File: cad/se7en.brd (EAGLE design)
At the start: 64 x 34 mm, 67 parts, among them CN1 MICROSD-EJECT, CN3 DO NOT PLACE, CN4 DO NOT PLACE, CN5 DO NOT PLACE, CN8 HEADER-1X2-THM, Q1 FDC6392S, SW1 SWITCHKMR211, SW2 SWITCHKMR211, U1 ATSAMS70, U2 MCP73831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

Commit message: tweak
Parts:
- CN2: device adafruit:JST-PH-2-SMT-RA -> jaw:JST-PH-2-SMT-RA
- USB1: value CON-USB-F-MICRO-B -> USB-F-B-MICRO-B-192; device dp_devices:CONN_USB_MICRO-B -> jaw:USB-MICRO-B-192
- turned CN2 to 270 degrees

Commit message: usb improve Zd
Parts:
- CN8: value HEADER-1X2-THM -> HEADER-1X2M254; device jaw:HEADER-1X2-THM -> jaw:HEADER-1X2-THM-TIGHT
- moved C1 0.50 mm to (89.0, 64.5)
- moved C13 0.50 mm to (95.0, 64.5)
- moved C16 0.50 mm to (87.0, 64.5)
- moved C17 0.50 mm to (92.5, 64.5)
- moved C2 0.50 mm to (83.5, 64.5)
- moved C3 0.50 mm to (91.0, 64.5)
- moved C5 0.50 mm to (77.5, 64.5)
- moved L1 0.50 mm to (88.0, 64.5)
- moved L2 0.50 mm to (84.5, 64.5)
- moved L3 0.50 mm to (90.0, 64.5)
- moved R2 0.50 mm to (78.5, 64.5)
- moved X1 0.50 mm to (80.5, 63.5)
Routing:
- net VCC: track 55.0 -> 53.9 mm
- net N$7: track 10.9 -> 10.2 mm
- net USBDP: track 28.0 -> 27.3 mm
- net USBDM: track 28.0 -> 27.3 mm
- net N$6: track 6.35 -> 5.79 mm
- net N$3: track 4.50 -> 4.00 mm
- net N$2: track 4.91 -> 4.41 mm
- net N$1: track 4.71 -> 4.21 mm
- net GND: track 99.8 -> 100.1 mm, vias 91 -> 107
- added copper zone on layer 1, net N$22
- added copper zone on layer 1, net N$23
- added copper zone on layer 16, net N$24
- added copper zone on layer 16, net N$25
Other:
- board text added: "Cortex M7 Much FAST!"
- board text added: "JAW 2016"
- board text added: "WOW, so many pins!"
- board text added: "diag"
- board text removed: "serial"

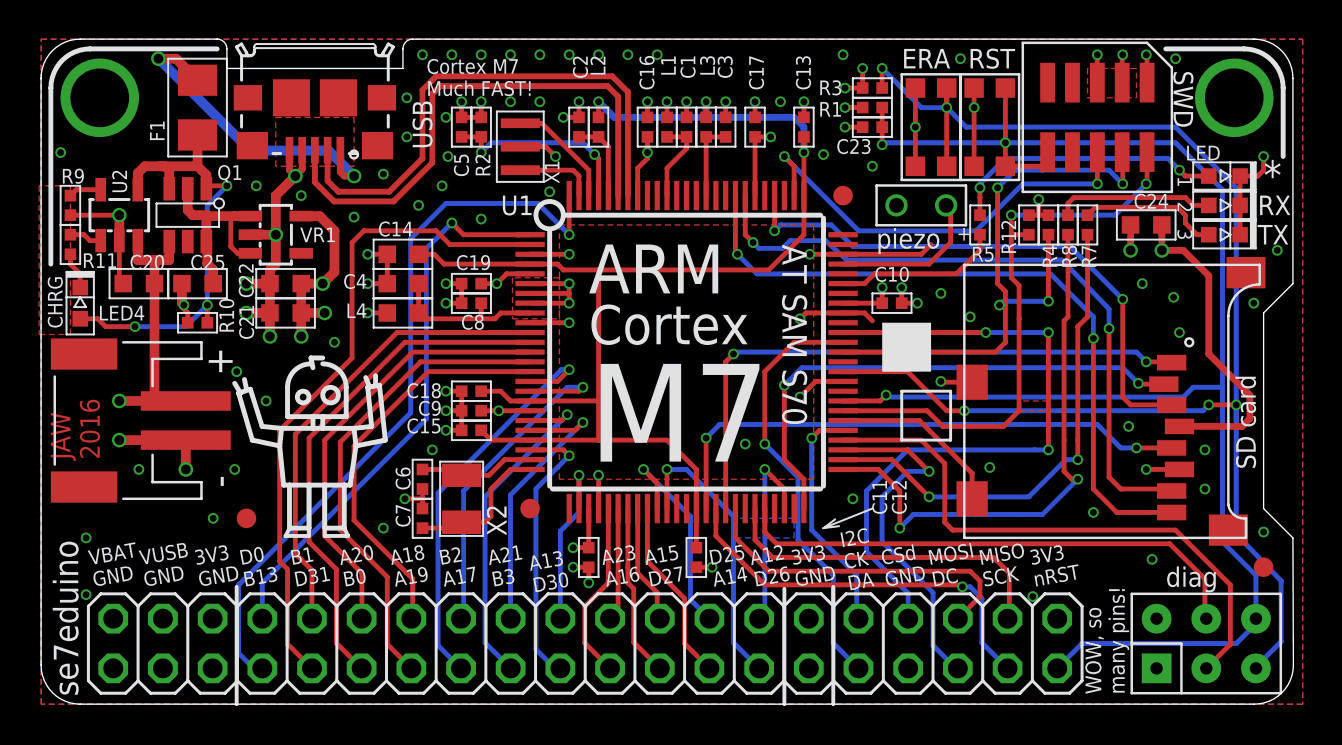
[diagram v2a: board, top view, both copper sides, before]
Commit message: drop vbat pins, add more io
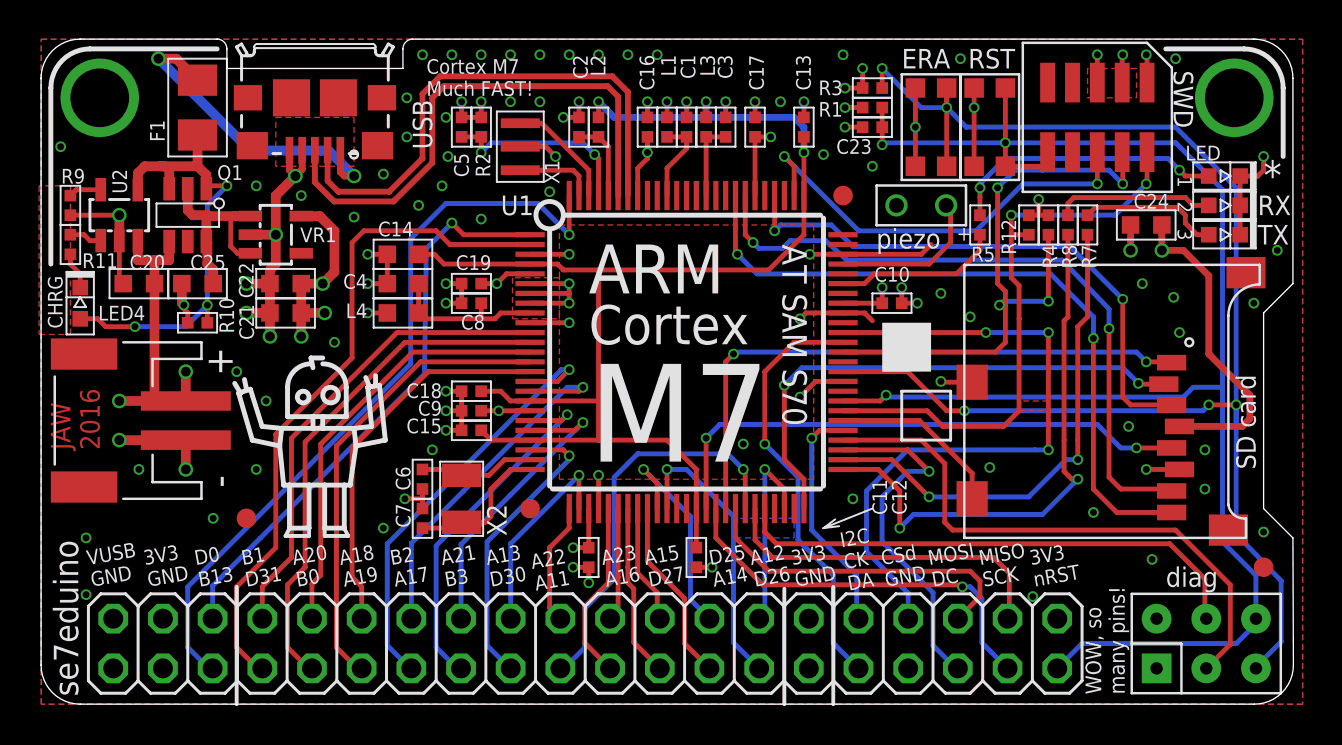
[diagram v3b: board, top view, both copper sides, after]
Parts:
- CN8: value HEADER-1X2M254 -> DO NOT PLACE
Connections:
- new net PINA11: CN5.22, U1.44
- new net PINA22: CN5.21, U1.26
- net GND: no longer CN5.36
- net PINA13: now also CN5.23; no longer CN5.21
- net PINA17: now also CN5.28; no longer CN5.26
- net PINA18: now also CN5.29; no longer CN5.27
- net PINA19: now also CN5.30; no longer CN5.28
- net PINA20: now also CN5.31; no longer CN5.29
- net PINA21: now also CN5.25; no longer CN5.23
- net PINB0: now also CN5.32; no longer CN5.30
- net PINB1: now also CN5.33; no longer CN5.31
- net PINB13: now also CN5.36; no longer CN5.34
- net PINB2: now also CN5.27; no longer CN5.25
- net PINB3: now also CN5.26; no longer CN5.24
- net PIND0: now also CN5.35; no longer CN5.33
- net PIND30: now also CN5.24; no longer CN5.22
- net PIND31: now also CN5.34; no longer CN5.32
- net VBAT: no longer CN5.39
- net VCC: now also CN5.37; no longer CN5.35
- net VUSB: now also CN5.39; no longer CN5.37
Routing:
- net PINA11: track 0.00 -> 20.5 mm, vias 0 -> 1
- net VBAT: track 30.2 -> 16.6 mm, vias 1 -> 2
- net PINA22: track 0.00 -> 6.27 mm
- net PINA17: track 21.0 -> 22.1 mm
- net PINB3: track 17.3 -> 18.4 mm
- net PINB2: track 17.7 -> 18.7 mm
- net PINA13: track 9.42 -> 10.5 mm
- net PINA21: track 14.4 -> 15.5 mm
- net PINA18: track 20.7 -> 19.6 mm
- net PIND0: track 28.5 -> 29.5 mm
- net PINB13: track 37.9 -> 38.8 mm
- net PIND31: track 33.6 -> 34.5 mm
- net PIND30: track 14.4 -> 15.3 mm
- net PINA19: track 24.5 -> 23.7 mm
- net PINA20: track 22.3 -> 21.8 mm
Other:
- board text added: "A22 A11"
- board text added: "JAW 2016-07"
- board text added: "SE7EDUINO Rev. 1"
- board text removed: "JAW 2016-05"
- board text removed: "SE7EDUINO Rev. 0"
- board text removed: "VBAT GND"

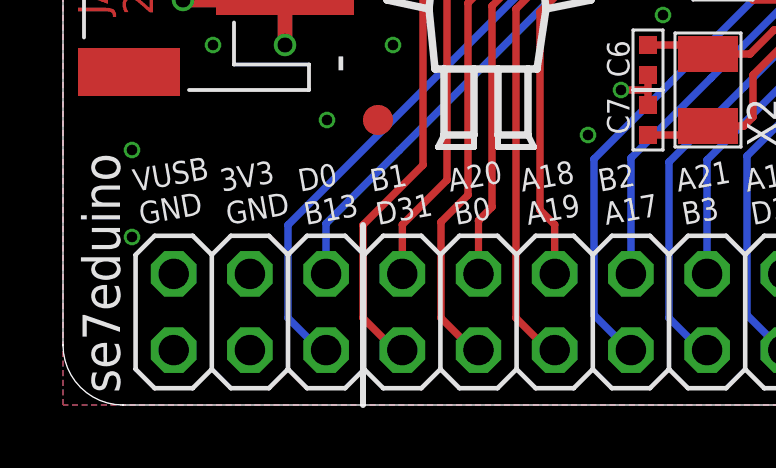
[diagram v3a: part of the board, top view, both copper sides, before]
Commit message: brighten green
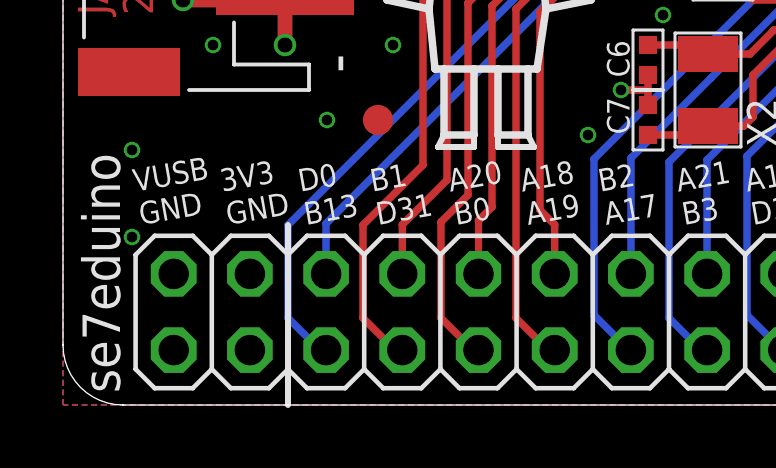
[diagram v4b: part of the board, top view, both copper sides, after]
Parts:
- R8: value 1k -> 470
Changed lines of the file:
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@@
 <grid distance="0.1" unitdist="mm" unit="mm" style="lines" multiple="5" display="yes" altdistance="0.025" altunitdist="inch" altunit="inch"/>
 <layers>
-<layer number="1" name="Top" color="4" fill="1" visible="no" active="yes"/>
+<layer number="1" name="Top" color="4" fill="1" visible="yes" active="yes"/>
 <layer number="2" name="Route2" color="6" fill="1" visible="no" active="yes"/>
 <layer number="3" name="Route3" color="4" fill="3" visible="no" active="no"/>
 <layer number="14" name="Route14" color="1" fill="6" visible="no" active="no"/>
 <layer number="15" name="Route15" color="13" fill="1" visible="no" active="yes"/>
-<layer number="16" name="Bottom" color="1" fill="1" visible="no" active="yes"/>
+<layer number="16" name="Bottom" color="1" fill="1" visible="yes" active="yes"/>
 <layer number="17" name="Pads" color="2" fill="1" visible="yes" active="yes"/>
 <layer number="18" name="Vias" color="2" fill="1" visible="yes" active="yes"/>
@@
 <text x="84" y="47.4" size="5" layer="21" ratio="15">M7</text>
 <text x="93.9" y="58.5" size="1.25" layer="21" ratio="15" rot="SR270">AT SAM S70</text>
-<wire x1="66" y1="41" x2="66" y2="35" width="0.2" layer="21"/>
+<wire x1="63.5" y1="41" x2="63.5" y2="35" width="0.2" layer="21"/>
 <wire x1="94" y1="40.9" x2="94" y2="35" width="0.2" layer="21"/>
 <wire x1="96.5" y1="41" x2="96.5" y2="35" width="0.2" layer="21"/>
@@
 <attribute name="VALUE" x="109" y="60.3" size="1" layer="27" font="vector" ratio="10" rot="R270"/>
 </element>
-<element name="R8" library="jaw" package="SMD0402" value="1k" x="108.5" y="59.5" smashed="yes" rot="R270">
+<element name="R8" library="jaw" package="SMD0402" value="470" x="108.5" y="59.5" smashed="yes" rot="R270">
 <attribute name="NAME" x="108.2" y="58.5" size="0.75" layer="25" font="vector" ratio="10" rot="R270"/>
 <attribute name="VALUE" x="108" y="60.3" size="1" layer="27" font="vector" ratio="10" rot="R270"/>
